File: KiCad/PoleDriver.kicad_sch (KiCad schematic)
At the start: 2 parts, among them Q1 SP60N10GDNK

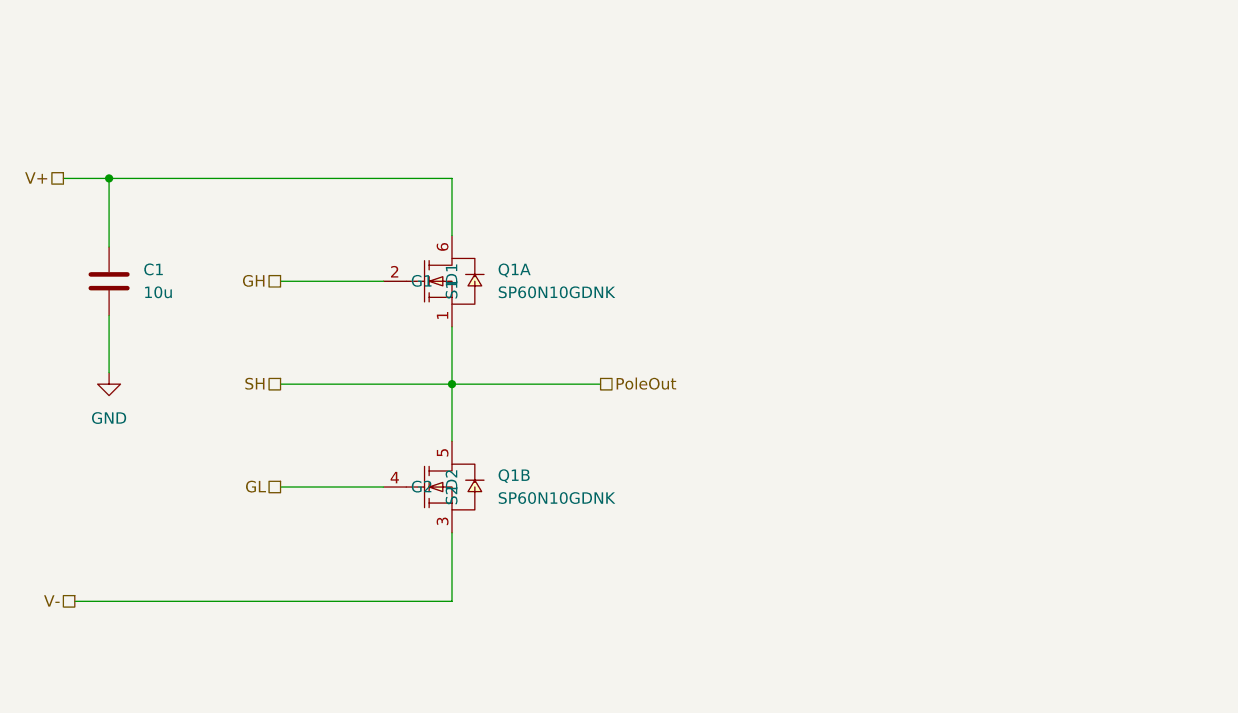
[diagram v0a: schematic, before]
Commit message: High current drive routing
Add TDSON-8 3D models and footprint (.step, .wrl, .kicad_mod) and update easyeda2kicad library; modify KiCad schematic sheets (DriverStage.kicad_sch, PoleDriver.kicad_sch, simpleFOC Dual Motor Controller.kicad_sch) to reposition symbols/wires, add connector symbol instances, and refresh UUIDs and component references (e.g. C2/C3/U2 -> C202/C201/U201). Also update PCB and project files to reflect schematic changes so footprints and global labels stay in sync.
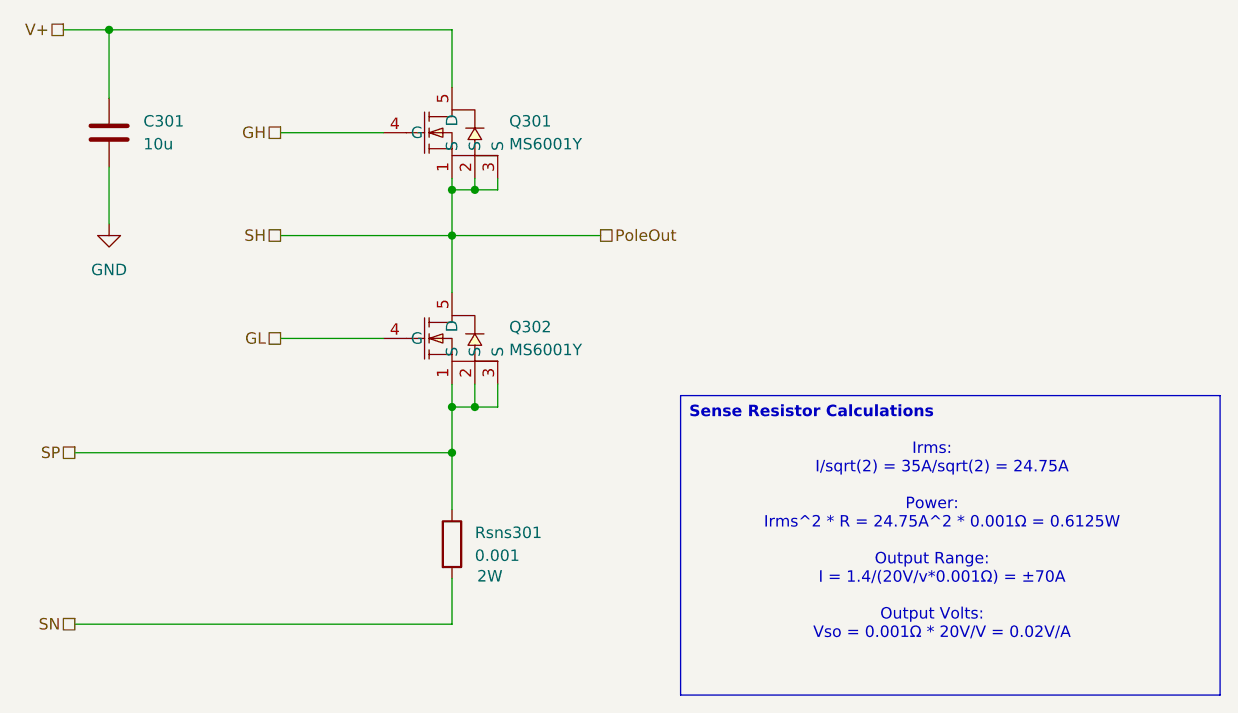
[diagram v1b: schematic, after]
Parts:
- removed Q1: SP60N10GDNK, easyeda2kicad:DFN-8_L5.5-W5.2-P1.27-LS6.0-BL-EP2, symbol easyeda2kicad:SP60N10GDNK
- added Q301, Q302: MS6001Y, easyeda2kicad:TDSON-8_L5.9-W5.2-P1.27-BL, symbol easyeda2kicad:MS6001Y
- added Rsns301: 0.001, Resistor_SMD:R_2512_6332Metric, symbol Device:R
- C301: renamed from C1; footprint (none) -> Capacitor_SMD:C_1206_3216Metric
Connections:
- net GH: now also Q301.4 (G)
- net GL: now also Q302.4 (G)
- net PoleOut: now also Q301.1 (S), Q301.2 (S), Q301.3 (S), Q302.5 (D)
- net V+: now also Q301.5 (D)
- new net SN: Rsns301.2
- new net SP: Q302.1 (S), Q302.2 (S), Q302.3 (S), Rsns301.1
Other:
- note added: "Irms: I/sqrt(2) = 35A/sqrt(2) = 24.75A Power: Irms^2 * R = 24.75A^2 * 0.001Ω = 0.6125W Output Range: I = 1.4/(20V/v*0.001Ω) = ±70A Output Volts: Vso = 0.001Ω * 20V/V = 0.02V/A"
- title: (none) -> Motor Pole Half-Bridge
- moved on the sheet: C301

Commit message: added board design rules
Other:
- note added: "Irms: I/sqrt(2) = 35A/sqrt(2) = 24.75A Power: Irms^2 * R = 24.75A^2 * 0.001Ω = 0.6125W Output Range: I = 1.4/(40V/V*0.001Ω) = ±35A Output Volts: Vso = 0.001Ω * 40V/V = 0.040V/A"
- note removed: "Irms: I/sqrt(2) = 35A/sqrt(2) = 24.75A Power: Irms^2 * R = 24.75A^2 * 0.001Ω = 0.6125W Output Range: I = 1.4/(20V/v*0.001Ω) = ±70A Output Volts: Vso = 0.001Ω * 20V/V = 0.02V/A"
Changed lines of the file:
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@@
 		(title "Motor Pole Half-Bridge")
 	)
-	(text "Irms:\n	I/sqrt(2) = 35A/sqrt(2) = 24.75A\n\nPower:\n	Irms^2 * R = 24.75A^2 * 0.001Ω = 0.6125W\n\nOutput Range:\n	I = 1.4/(20V/v*0.001Ω) = ±70A\n\nOutput Volts:\n	Vso = 0.001Ω * 20V/V = 0.02V/A"
+	(text "Irms:\n	I/sqrt(2) = 35A/sqrt(2) = 24.75A\n\nPower:\n	Irms^2 * R = 24.75A^2 * 0.001Ω = 0.6125W\n\nOutput Range:\n	I = 1.4/(40V/V*0.001Ω) = ±35A\n\nOutput Volts:\n	Vso = 0.001Ω * 40V/V = 0.040V/A"
 		(exclude_from_sim no)
 		(at 153.67 78.486 0)

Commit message: Finished wiring motor drive circuitry
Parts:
- added R301, R302: 47k, symbol Device:R_Small
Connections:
- net GH: now also R302.1
- net GL: now also R301.1
- net PoleOut: now also R302.2
- net SP: now also R301.2

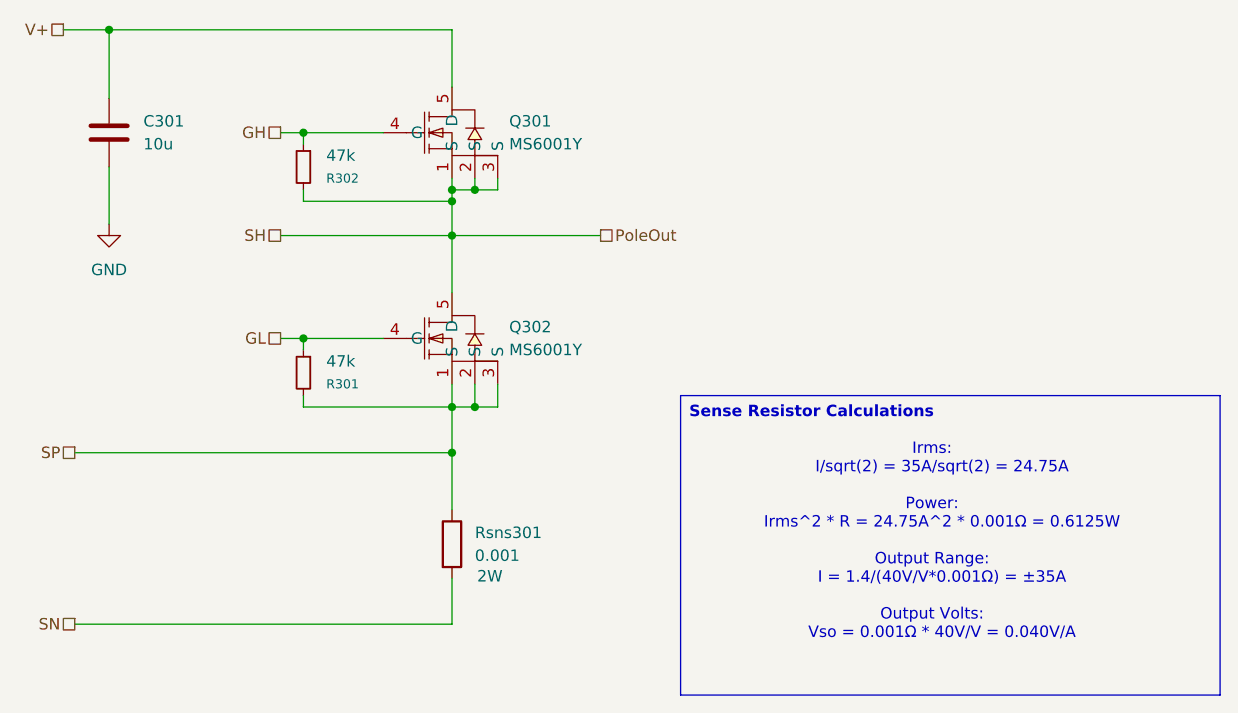
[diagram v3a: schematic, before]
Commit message: rewired the board with smaller mosfets
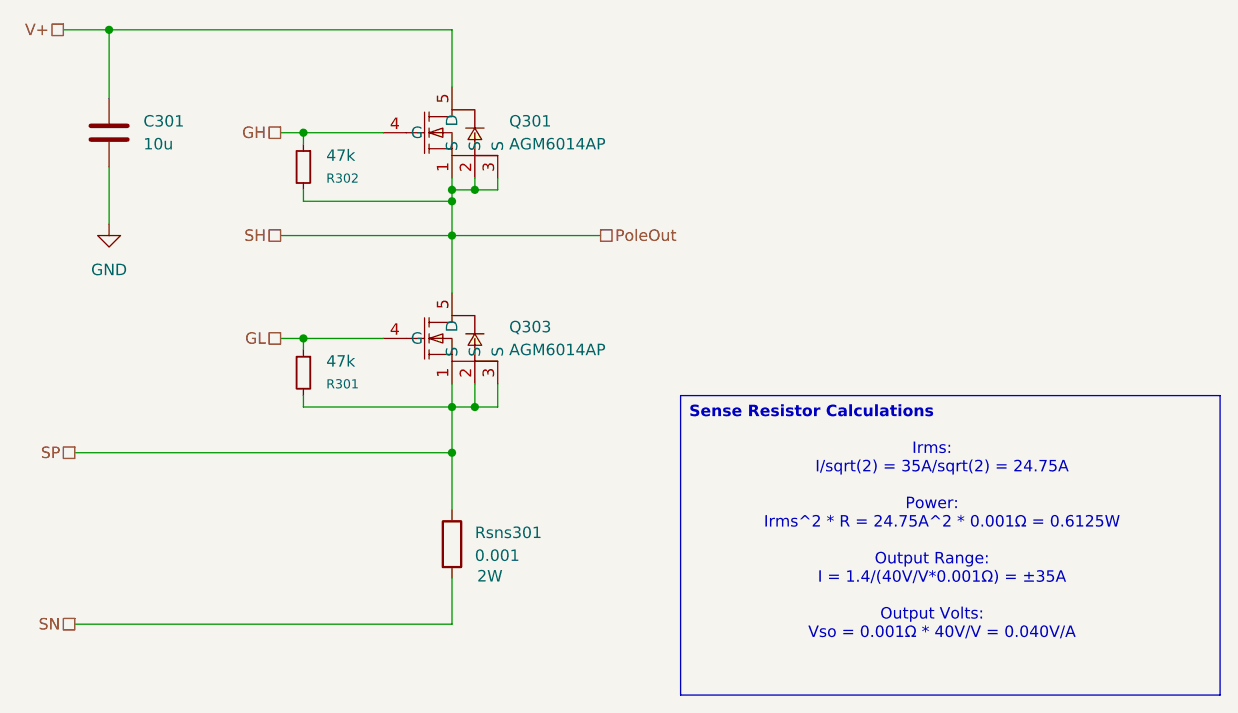
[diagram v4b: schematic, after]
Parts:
- removed Q301, Q302: MS6001Y, easyeda2kicad:TDSON-8_L5.9-W5.2-P1.27-BL, symbol easyeda2kicad:MS6001Y
- added Q301, Q303: AGM6014AP, easyeda2kicad:PDFN-8_L3.1-W3.0-P0.65-LS3.3-BL, symbol easyeda2kicad:AGM6014AP
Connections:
- net GH: now also Q301.4 (G)
- net GL: now also Q303.4 (G)
- net PoleOut: now also Q301.1 (S), Q301.2 (S), Q301.3 (S), Q303.5 (D)
- net SP: now also Q303.1 (S), Q303.2 (S), Q303.3 (S)
- net V+: now also Q301.5 (D)
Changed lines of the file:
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@@
-	)
-	(symbol
-		(lib_id "easyeda2kicad:MS6001Y")
-		(at 99.06 55.88 0)
-		(unit 1)
-		(body_style 1)
-		(exclude_from_sim no)
-		(in_bom yes)
-		(on_board yes)
-		(in_pos_files yes)
-		(dnp no)
-		(fields_autoplaced yes)
-		(property "Reference" "Q302"
-			(at 106.68 54.6099 0)
-			(show_name no)
-			(do_not_autoplace no)
-			(effects
-				(font
-					(size 1.27 1.27)
-				)
-				(justify left)
-			)
-		)
-		(property "Value" "MS6001Y"
-			(at 106.68 57.1499 0)
-			(show_name no)
-			(do_not_autoplace no)
-			(effects
-				(font
-					(size 1.27 1.27)
-				)
-				(justify left)
-			)
-		)
-		(property "Footprint" "easyeda2kicad:TDSON-8_L5.9-W5.2-P1.27-BL"
-			(at 99.06 68.58 0)
-			(hide yes)
-			(show_name no)
-			(do_not_autoplace no)
-			(effects
-				(font
-					(size 1.27 1.27)
-				)
-			)
-		)
-		(property "Datasheet" "https://www.lcsc.com/datasheet/C17702010.pdf"
-			(at 99.06 71.12 0)
-			(hide yes)
-			(show_name no)
-			(do_not_autoplace no)
-			(effects
-				(font
-					(size 1.27 1.27)
-				)
-			)
-		)
-		(property "Description" ""
-			(at 99.06 55.88 0)
-			(hide yes)
-			(show_name no)
-			(do_not_autoplace no)
-			(effects
-				(font
-					(size 1.27 1.27)
-				)
-			)
-		)
-		(property "Manufacturer" "MP(美禄科技)"
-			(at 99.06 73.66 0)
-			(hide yes)
-			(show_name no)
-			(do_not_autoplace no)
-			(effects
-				(font
-					(size 1.27 1.27)
-				)
-			)
-		)
-		(property "MPN" "MS6001Y"
-			(at 99.06 76.2 0)
-			(hide yes)
-			(show_name no)
-			(do_not_autoplace no)
-			(effects
-				(font
-					(size 1.27 1.27)
-				)
-			)
-		)
-		(property "LCSC Part" "C17702010"
-			(at 99.06 78.74 0)
-			(hide yes)
-			(show_name no)
-			(do_not_autoplace no)
-			(effects
-				(font
-					(size 1.27 1.27)
-				)
-			)
-		)
-		(pin "2"
-		)
-		(pin "4"
-		)
-		(pin "3"
-		)
-		(pin "1"
-		)
-		(pin "5"
-		)
-		(instances
-			(project "simpleFOC Dual Motor Controller"
-				(path "/0dffc378-5905-459a-b0cb-e8e514a8bbef/de390f81-41fc-4236-a904-44260774a171/20b87812-a82e-42f6-920a-0aca573365c0"
-					(reference "Q502")
-					(unit 1)
-				)
-				(path "/0dffc378-5905-459a-b0cb-e8e514a8bbef/de390f81-41fc-4236-a904-44260774a171/cd26c950-3a70-43f9-bc93-52ca2ff7311f"
-					(reference "Q302")
-					(unit 1)
-				)
-				(path "/0dffc378-5905-459a-b0cb-e8e514a8bbef/de390f81-41fc-4236-a904-44260774a171/ee00243c-0671-4d24-ad12-35a8d122e435"
-					(reference "Q402")
-					(unit 1)
-				)
-				(path "/0dffc378-5905-459a-b0cb-e8e514a8bbef/e842f42e-62e8-4809-9799-e9078ef99b24/20b87812-a82e-42f6-920a-0aca573365c0"
-					(reference "Q802")
-					(unit 1)
-				)
-				(path "/0dffc378-5905-459a-b0cb-e8e514a8bbef/e842f42e-62e8-4809-9799-e9078ef99b24/cd26c950-3a70-43f9-bc93-52ca2ff7311f"
-					(reference "Q902")
-					(unit 1)
-				)
-				(path "/0dffc378-5905-459a-b0cb-e8e514a8bbef/e842f42e-62e8-4809-9799-e9078ef99b24/ee00243c-0671-4d24-ad12-35a8d122e435"
-					(reference "Q702")
-					(unit 1)
-				)
-			)
-		)
 	)
 	(symbol
@@
 	)
 	(symbol
-		(lib_id "easyeda2kicad:MS6001Y")
+		(lib_id "easyeda2kicad:AGM6014AP")
 		(at 99.06 33.02 0)
 		(unit 1)
@@
 			)
 		)
-		(property "Value" "MS6001Y"
+		(property "Value" "AGM6014AP"
 			(at 106.68 34.2899 0)
 			(show_name no)
@@
 			)
 		)
-		(property "Footprint" "easyeda2kicad:TDSON-8_L5.9-W5.2-P1.27-BL"
+		(property "Footprint" "easyeda2kicad:PDFN-8_L3.1-W3.0-P0.65-LS3.3-BL"
 			(at 99.06 45.72 0)
 			(hide yes)
@@
 			)
 		)
-		(property "Datasheet" "https://www.lcsc.com/datasheet/C17702010.pdf"
+		(property "Datasheet" "https://www.lcsc.com/datasheet/C6719405.pdf"
 			(at 99.06 48.26 0)
 			(hide yes)
@@
 			)
 		)
-		(property "Manufacturer" "MP(美禄科技)"
+		(property "Manufacturer" "AGMSEMI(芯控源)"
 			(at 99.06 50.8 0)
 			(hide yes)
@@
 			)
 		)
-		(property "MPN" "MS6001Y"
+		(property "MPN" "AGM6014AP"
 			(at 99.06 53.34 0)
 			(hide yes)
@@
 			)
 		)
-		(property "LCSC Part" "C17702010"
+		(property "LCSC Part" "C6719405"
 			(at 99.06 55.88 0)
 			(hide yes)
@@
 		(pin "4"
 		)
+		(pin "5"
+		)
+		(pin "1"
+		)
 		(pin "3"
-		)
-		(pin "1"
-		)
-		(pin "5"
 		)
 		(instances
@@
 					(unit 1)
 				)
+			)
+		)
+	)
+	(symbol
+		(lib_id "easyeda2kicad:AGM6014AP")
+		(at 99.06 55.88 0)
+		(unit 1)
+		(body_style 1)
+		(exclude_from_sim no)
+		(in_bom yes)
+		(on_board yes)
+		(in_pos_files yes)
+		(dnp no)
+		(fields_autoplaced yes)
+		(property "Reference" "Q303"
+			(at 106.68 54.6099 0)
+			(show_name no)
+			(do_not_autoplace no)
+			(effects
+				(font
+					(size 1.27 1.27)
+				)
+				(justify left)
+			)
+		)
+		(property "Value" "AGM6014AP"
+			(at 106.68 57.1499 0)
+			(show_name no)
+			(do_not_autoplace no)
+			(effects
+				(font
+					(size 1.27 1.27)
+				)
+				(justify left)
+			)
+		)
+		(property "Footprint" "easyeda2kicad:PDFN-8_L3.1-W3.0-P0.65-LS3.3-BL"
+			(at 99.06 68.58 0)
+			(hide yes)
+			(show_name no)
+			(do_not_autoplace no)
+			(effects
+				(font
+					(size 1.27 1.27)
+				)
+			)
+		)
+		(property "Datasheet" "https://www.lcsc.com/datasheet/C6719405.pdf"
+			(at 99.06 71.12 0)
+			(hide yes)
+			(show_name no)
+			(do_not_autoplace no)
+			(effects
+				(font
+					(size 1.27 1.27)
+				)
+			)
+		)
+		(property "Description" ""
+			(at 99.06 55.88 0)
+			(hide yes)
+			(show_name no)
+			(do_not_autoplace no)
+			(effects
+				(font
+					(size 1.27 1.27)
+				)
+			)
+		)
+		(property "Manufacturer" "AGMSEMI(芯控源)"
+			(at 99.06 73.66 0)
+			(hide yes)
+			(show_name no)
+			(do_not_autoplace no)
+			(effects
+				(font
+					(size 1.27 1.27)
+				)
+			)
+		)
+		(property "MPN" "AGM6014AP"
+			(at 99.06 76.2 0)
+			(hide yes)
+			(show_name no)
+			(do_not_autoplace no)
+			(effects
+				(font
+					(size 1.27 1.27)
+				)
+			)
+		)
+		(property "LCSC Part" "C6719405"
+			(at 99.06 78.74 0)
+			(hide yes)
+			(show_name no)
+			(do_not_autoplace no)
+			(effects
+				(font
+					(size 1.27 1.27)
+				)
+			)
+		)
+		(pin "2"
+		)
+		(pin "4"
+		)
+		(pin "5"
+		)
+		(pin "1"
+		)
+		(pin "3"
+		)
+		(instances
+			(project "simpleFOC Dual Motor Controller"
+				(path "/0dffc378-5905-459a-b0cb-e8e514a8bbef/de390f81-41fc-4236-a904-44260774a171/20b87812-a82e-42f6-920a-0aca573365c0"
+					(reference "Q503")
+					(unit 1)
+				)
+				(path "/0dffc378-5905-459a-b0cb-e8e514a8bbef/de390f81-41fc-4236-a904-44260774a171/cd26c950-3a70-43f9-bc93-52ca2ff7311f"
+					(reference "Q303")
+					(unit 1)
+				)
+				(path "/0dffc378-5905-459a-b0cb-e8e514a8bbef/de390f81-41fc-4236-a904-44260774a171/ee00243c-0671-4d24-ad12-35a8d122e435"
+					(reference "Q403")
+					(unit 1)
+				)
+				(path "/0dffc378-5905-459a-b0cb-e8e514a8bbef/e842f42e-62e8-4809-9799-e9078ef99b24/20b87812-a82e-42f6-920a-0aca573365c0"
+					(reference "Q803")
+					(unit 1)
+				)
+				(path "/0dffc378-5905-459a-b0cb-e8e514a8bbef/e842f42e-62e8-4809-9799-e9078ef99b24/cd26c950-3a70-43f9-bc93-52ca2ff7311f"
+					(reference "Q903")
+					(unit 1)
+				)
+				(path "/0dffc378-5905-459a-b0cb-e8e514a8bbef/e842f42e-62e8-4809-9799-e9078ef99b24/ee00243c-0671-4d24-ad12-35a8d122e435"
+					(reference "Q703")
+					(unit 1)
+				)
